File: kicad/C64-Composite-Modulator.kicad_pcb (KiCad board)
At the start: 2 copper layers, 63.5 x 60 mm, 56 parts, among them J1 Conn_01x04_Male, J2 Conn_01x04_Male, J3 Conn_01x04_Male, J4 Conn_01x04_Male, Q1 BC847B, Q2 BC847B, U1 78L05

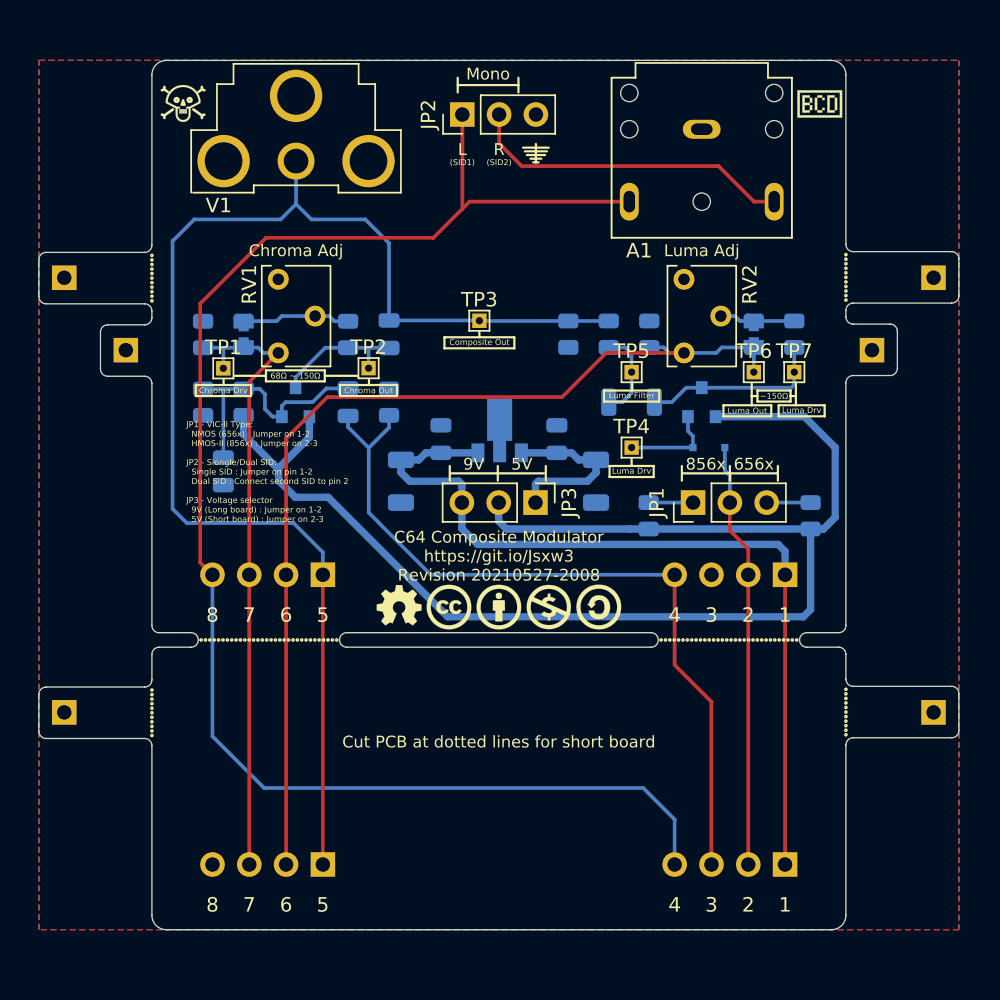
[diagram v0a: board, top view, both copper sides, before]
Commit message: Rev 20210531-2143 - Bug Fix
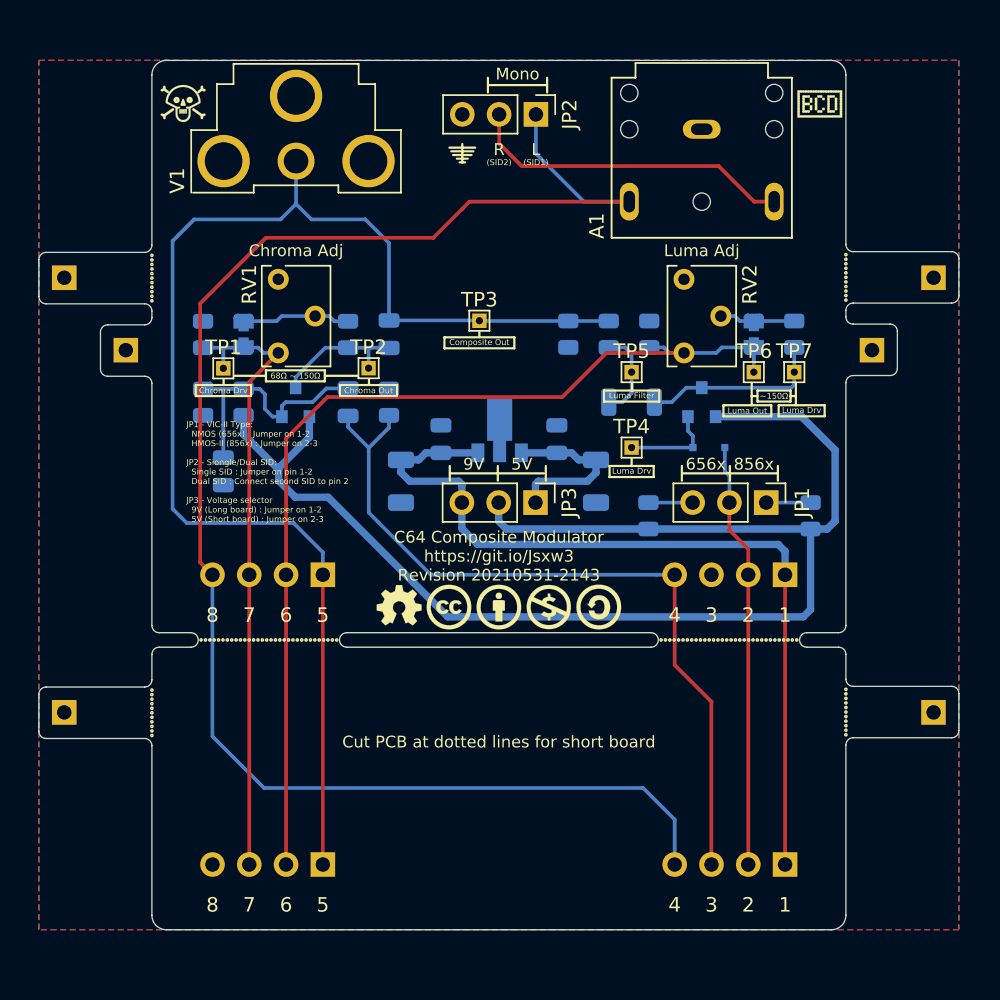
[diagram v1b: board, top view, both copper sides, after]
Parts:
- moved R7 11.2 mm to (151.1, 106.4)
- moved R6 11.2 mm to (162.3, 106.4)
- moved JP2 5.08 mm to (143.4, 78.7), turned to 270 degrees
- moved JP1 5.05 mm to (159.2, 105.5), turned to 270 degrees
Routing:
- net AudioIn: track 106.7 -> 110.7 mm
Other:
- board text added: "C64 Composite Modulator https://git.io/Jsxw3 Revision 20210531-2143"
- board text removed: "C64 Composite Modulator https://git.io/Jsxw3 Revision 20210527-2008"

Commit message: Revision 20220130-1040
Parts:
- removed B1: RV1 Bypass, C64 Composite Modulator:J_0805_2012Metric
- removed B2: RV2 Bypass, C64 Composite Modulator:J_0805_2012Metric
- removed BCD1: BCD(DOT), BCD:BCD_LOGO_DOT-xxxsmall
- removed BY1: CC-BY, BCD:CC-BY-xxxsmall
- removed CC1: CC, BCD:CC-Logo-xxxsmall
- removed Danger1: Danger, BCD:Danger-xxxsmall
- removed J1, J2, J3, J4: Conn_01x04_Male, C64 Composite Modulator:mill-max-800-10-004-10-001000
- removed JP3: Jumper_3_Open, Connector_PinHeader_2.54mm:PinHeader_1x03_P2.54mm_Vertical
- removed LB1, LB2, LB3, LB4, SB1, SB2: Conn_01x01_Male, C64 Composite Modulator:mill-max-800-10-001-10-001000
- removed NC1: CC-NC, BCD:CC-NC-xxxsmall
- removed OSHW1: OSHW, BCD:OSHW-xxxsmall
- removed SA1: CC-SA, BCD:CC-SA-xxxsmall
- added CLB1: Modulator_Board_To_Long_Board, C64 Composite Modulator:Modulator to Long-Board support, F.Cu at (140.8, 105.4)
- added CSB1: Modulator_Board_To_Short_Board, C64 Composite Modulator:Modulator to Short-Board support, F.Cu at (140.8, 104.9)
- added G1: BCD_Logo, BeaupreCircuitDesign:BCD_Logo_5mm, F.Cu at (140.8, 93.7)
- added G2: ChickenLips, BeaupreCircuitDesign:ChickenLips_2.5mm, F.Cu at (137.0, 97.6)
- added G3: OpenSource_Hardware, BeaupreCircuitDesign:Open_Source_Hardware_2.5mm, F.Cu at (144.6, 97.6)
- added G4: Skull, BeaupreCircuitDesign:Skull_2.5mm, F.Cu at (140.8, 97.6)
- added G5: CreativeCommons, Creative_Common:CreativeCommons_2.5mm, F.Cu at (136.9, 111.5)
- added G6: CreativeCommons_Attribution, Creative_Common:CreativeCommons_Attribution_2.5mm, F.Cu at (139.5, 111.5)
- added G7: CreativeCommons_NonCommercial, Creative_Common:CreativeCommons_NonCommercial_2.5mm, F.Cu at (142.1, 111.5)
- added G8: CreativeCommons_ShareAlike, Creative_Common:CreativeCommons_ShareAlike_2.5mm, F.Cu at (144.7, 111.5)
- added TP8: TestPoint, TestPoint:TestPoint_THTPad_2.0x2.0mm_Drill1.0mm, F.Cu at (161.7, 100.4)
- added TV1: TestPoint, TestPoint:TestPoint_THTPad_2.0x2.0mm_Drill1.0mm, F.Cu at (140.8, 100.4)
- A1: value SJ1-3523N -> Conn_Coaxial; footprint C64 Composite Modulator:CUI_SJ1-3523N -> CUI_Devices:RCJ-013
- CO1: renamed from C7; footprint Capacitor_SMD:C_0805_2012Metric -> Capacitor_THT:C_Disc_D4.7mm_W2.5mm_P5.00mm; moved to F.Cu
- D1: value 1N4148 -> 1N4148WS
- L1: footprint Inductor_SMD:L_1206_3216Metric -> Inductor_SMD:L_0805_2012Metric
- Q1, Q2: value BC847B -> BC847C
- R1, R7: value 1K -> 1KΩ
- R10: value 75 -> 75Ω
- R11, R8, R9: value 150 -> 150Ω
- R2: value 3K3 -> 3K3Ω
- R3: value 5K6 -> 5K6Ω
- R4: value 68 -> 68Ω
- R5: value 220 -> 220Ω
- R6: value 470 -> 470Ω
- RV1: value 200 -> 1KΩ; footprint Potentiometer_THT:Potentiometer_Bourns_3266W_Vertical -> Potentiometer_THT:Potentiometer_Bourns_3296W_Vertical
- RV2: value 200 -> 500Ω; footprint Potentiometer_THT:Potentiometer_Bourns_3266W_Vertical -> Potentiometer_THT:Potentiometer_Bourns_3296W_Vertical
- TP1, TP2, TP3, TP4, TP5, TP6, TP7: footprint TestPoint:TestPoint_THTPad_1.0x1.0mm_Drill0.5mm -> TestPoint:TestPoint_THTPad_2.0x2.0mm_Drill1.0mm
- U1: value 78L05 -> 78L05G-AB3-R
- V1: footprint C64 Composite Modulator:CUI_RCJ-014 -> CUI_Devices:RCJ-014
- moved JP2 26.1 mm to (138.3, 104.3), turned to 90 degrees
- moved TP4 17.0 mm to (136.5, 91.3)
- moved C1 13.6 mm to (146.9, 108.6)
- moved C4 13.6 mm to (134.7, 108.6)
- moved R5 11.9 mm to (132.2, 95.4), turned to -90 degrees
- moved TP3 11.4 mm to (128.5, 96.3), turned to 180 degrees
- moved R6 10.8 mm to (151.5, 105.2), turned to -90 degrees
- moved R7 10.6 mm to (161.7, 105.2), turned to -90 degrees
- moved C3 10.4 mm to (137.1, 108.1), turned to -90 degrees
- moved TP2 10.4 mm to (121.4, 96.3), turned to 180 degrees
- moved C2 10.4 mm to (144.5, 108.1), turned to -90 degrees
- moved R1 10.3 mm to (129.1, 108.0), turned to -90 degrees
- moved C5 10.2 mm to (126.3, 108.0), turned to -90 degrees
- moved R3 9.89 mm to (123.6, 107.9)
- moved TP1 8.69 mm to (125.0, 104.3), turned to 180 degrees
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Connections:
- A1 pad 1: GND -> AudioIn
- A1 pad 2: AudioIn -> GND
- C5 pad 1: ChromaIn -> Net-(C5-Pad1)
- C5 pad 2: Net-(C5-Pad2) -> ChromaIn
- C6 pad 1: Net-(C6-Pad1) -> CompositeOut
- C6 pad 2: CompositeOut -> Net-(C6-Pad2)
- CO1 pad 1: Net-(C5-Pad2) -> Net-(C5-Pad1)
- JP1 pad 2: LumaIn -> Net-(D1-Pad2)
- JP2 pad 1: AudioIn -> Net-(C3-Pad1)
- JP2 pad 2: Net-(A1-Pad3) -> +5V
- JP2 pad 3: GND -> VCC
- Q1 pad 1: +5V -> Net-(C5-Pad1)
- Q1 pad 2: Net-(C5-Pad2) -> Net-(C6-Pad2)
- Q1 pad 3: Net-(C6-Pad1) -> +5V
- Q2 pad 1: +5V -> Net-(D1-Pad2)
- Q2 pad 2: Net-(D1-Pad2) -> Net-(L1-Pad2)
- Q2 pad 3: Net-(L1-Pad1) -> +5V
- R1 pad 1: ChromaIn -> GND
- R1 pad 2: GND -> ChromaIn
- R10 pad 2: Net-(L1-Pad1) -> Net-(L1-Pad2)
- R11 pad 1: LumaOut -> GND
- R11 pad 2: GND -> LumaOut
- R2 pad 2: Net-(C5-Pad2) -> Net-(C5-Pad1)
- R3 pad 1: Net-(C5-Pad2) -> Net-(C5-Pad1)
- R4 pad 2: Net-(C6-Pad1) -> Net-(C6-Pad2)
- R6 pad 1: +5V -> Net-(JP1-Pad1)
- R6 pad 2: Net-(JP1-Pad1) -> +5V
- R7 pad 1: +5V -> Net-(JP1-Pad3)
- R7 pad 2: Net-(JP1-Pad3) -> +5V
- R8 pad 2: Net-(L1-Pad2) -> Net-(L1-Pad1)
- R9 pad 1: GND -> CompositeOut
- R9 pad 2: CompositeOut -> GND
- RV1 pad 1: (no net) -> ChromaOut
- RV1 pad 3: ChromaOut -> unconnected-(RV1-Pad3)
- RV2 pad 1: (no net) -> LumaOut
- RV2 pad 3: LumaOut -> unconnected-(RV2-Pad3)
- TP1 pad 1: ChromaOut -> Net-(C5-Pad1)
- TP2 pad 1: Net-(C6-Pad1) -> Net-(C6-Pad2)
- TP3 pad 1: CompositeOut -> ChromaOut
- TP4 pad 1: Net-(D1-Pad2) -> CompositeOut
- TP5 pad 1: Net-(L1-Pad2) -> Net-(L1-Pad1)
- TP7 pad 1: Net-(L1-Pad1) -> Net-(L1-Pad2)
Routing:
- net +5V: track 95.4 -> 58.1 mm
- net Net-(A1-Pad3): track 22.7 -> 0.00 mm
- net Net-(C6-Pad2): track 0.00 -> 19.6 mm
- net CompositeOut: track 92.2 -> 72.7 mm
- net Net-(C5-Pad1): track 0.00 -> 18.2 mm
- net Net-(C5-Pad2): track 17.4 -> 0.00 mm
- net Net-(L1-Pad2): track 6.29 -> 19.7 mm
- net Net-(C6-Pad1): track 9.43 -> 0.00 mm
- net ChromaOut: track 42.9 -> 49.6 mm
- net VCC: track 58.5 -> 52.6 mm
- net Net-(L1-Pad1): track 12.7 -> 6.78 mm
- net LumaOut: track 68.6 -> 74.2 mm
- net LumaIn: track 29.5 -> 24.4 mm
- net Net-(D1-Pad2): track 6.51 -> 11.2 mm
- net Net-(C3-Pad1): track 12.0 -> 8.20 mm
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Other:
- board size 63.5 x 60 mm -> 64.8 x 64.9 mm
- net class Default removed
- net class Power removed
- board text added: "+5V"
- board text added: "68Ω ~ 150Ω"
- board text added: "Chroma Drive"
- board text added: "Cut PCB at dotted lines for C64C (Short) board"
- board text added: "JLCJLCJLCJLC"
- board text added: "LB"
- board text added: "LCD FIX"
- board text added: "Long board: 1-2 Short board: 2-3"
- board text added: "Luma Drive"
- board text added: "NMOS (656x): 1-2 HMOS-II (856x): 2-3"
- board text added: "SB"
- board text added: "https://github.com/beaupre-circuit-design/ C64 Composite Modulator Revision 20220130-1040"
- board text added: "~ 150Ω"
- board text removed: "(SID1)"
- board text removed: "(SID2)"
- board text removed: "1"
- board text removed: "2"
- board text removed: "3"
- board text removed: "4"
- board text removed: "5"
- board text removed: "6"
- board text removed: "68Ω ~~ 150Ω"
- board text removed: "7"
- board text removed: "8"
- board text removed: "C64 Composite Modulator https://git.io/Jsxw3 Revision 20210531-2143"
- board text removed: "Chroma Drv"
- board text removed: "Cut PCB at dotted lines for short board"
- board text removed: "JP1 - VIC-II Type: NMOS (656x) : Jumper on 1-2 HMOS-II (856x) : Jumper on 2-3 JP2 - Siongle/Dual SID: Single SID : Jumper on pin 1-2 Dual SID : Connect second SID to pin 2 JP3 - Voltage selector 9V (Long board) : Jumper on 1-2 5V (Short board) : Jumper on 2-3"
- board text removed: "L"
- board text removed: "Luma Drv"
- board text removed: "Luma Filter"
- board text removed: "Mono"
- board text removed: "R"
- board text removed: "~~150Ω"

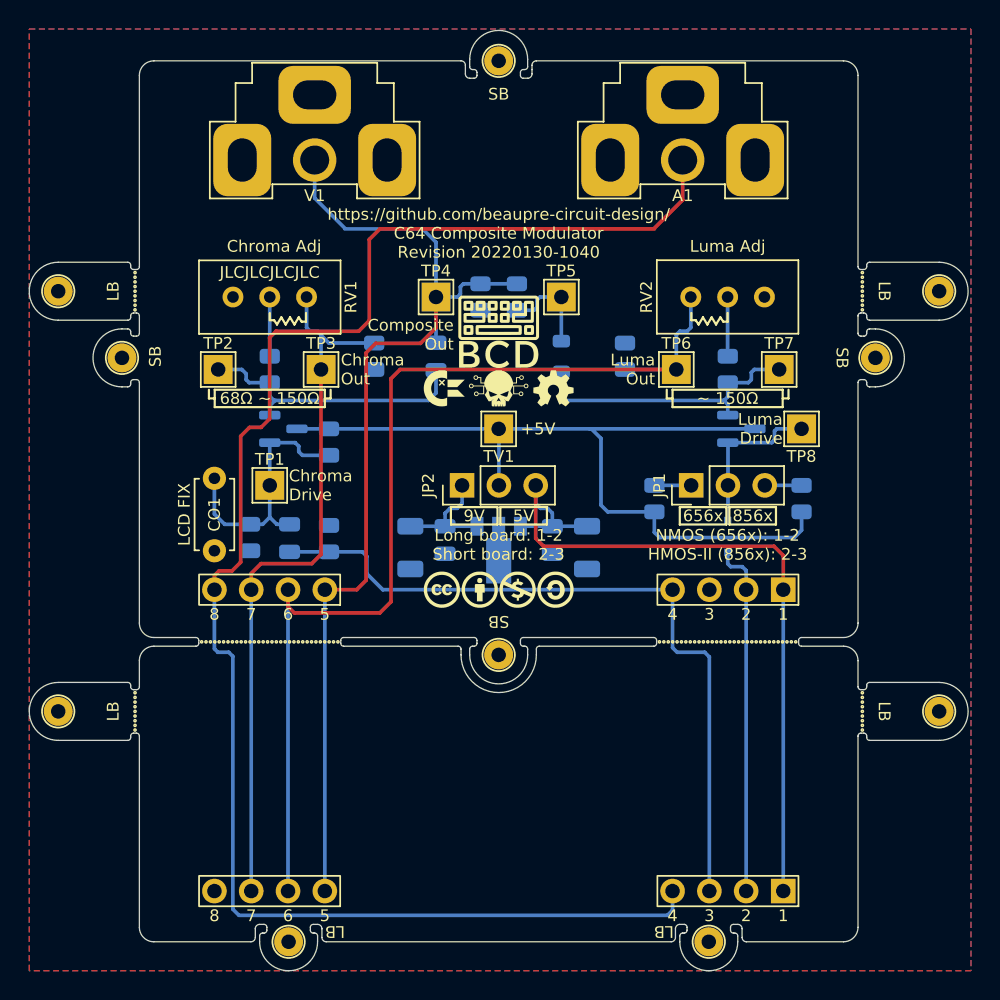
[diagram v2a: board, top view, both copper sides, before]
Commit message: Reduce the number of JLCPCB's extended parts
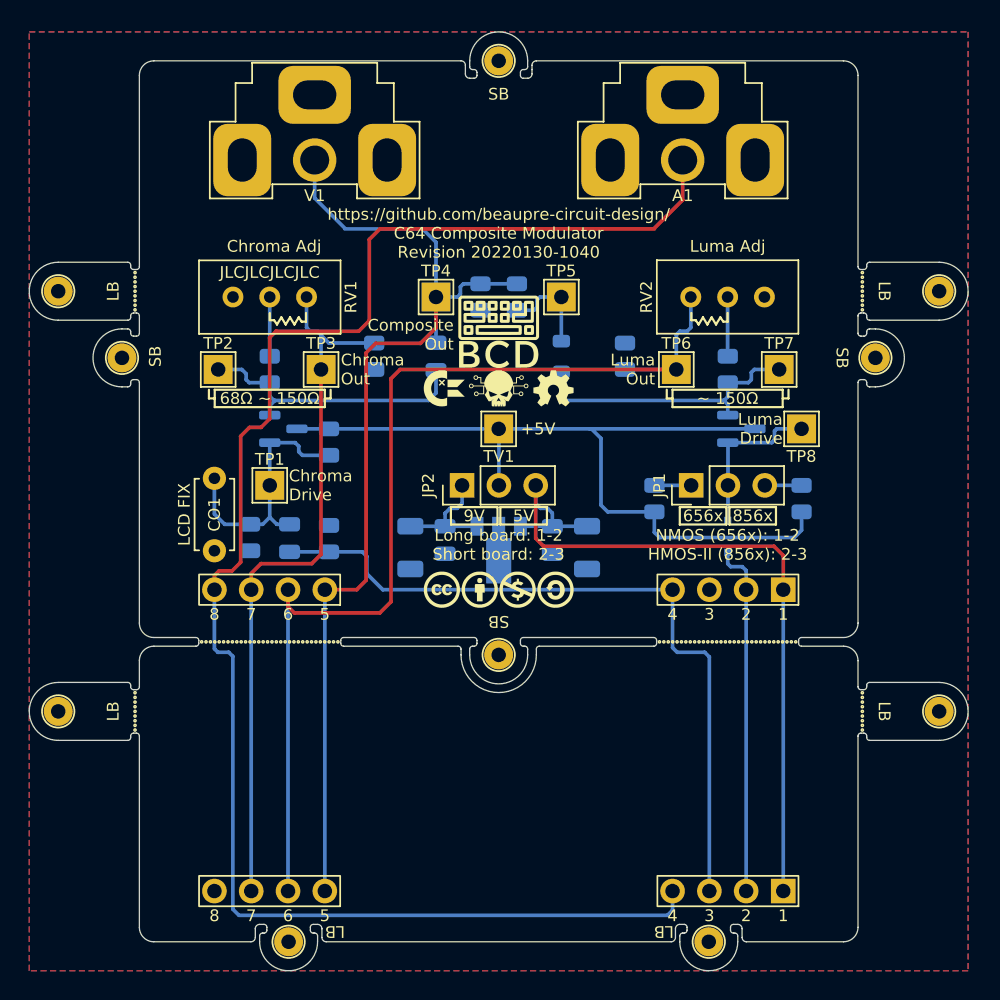
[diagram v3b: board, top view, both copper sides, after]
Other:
- board size 64.8 x 64.9 mm -> 64.8 x 64.8 mm

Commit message: Updated images and release notes
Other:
- board text removed: "Cut PCB at dotted lines for C64C (Short) board"
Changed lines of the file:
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@@
   (gr_line (start 165.582 113.82795) (end 165.582 97.22795) (layer "Edge.Cuts") (width 0.0381))
   (gr_arc (start 116.982 135.82795) (mid 116.274893 135.535057) (end 115.982 134.82795) (layer "Edge.Cuts") (width 0.0381))
-  (gr_text "Cut PCB at dotted lines for C64C (Short) board" (at 140.78199 125.62795) (layer "B.SilkS")
-    (effects (font (size 0.8128 0.8128) (thickness 0.1524)) (justify mirror))
-  )
   (gr_text "5V" (at 142.5039 106.42795) (layer "F.SilkS")
     (effects (font (size 0.8128 0.8128) (thickness 0.1524)))
